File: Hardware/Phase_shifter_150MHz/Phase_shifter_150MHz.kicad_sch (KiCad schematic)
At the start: 19 parts, among them J1 SMA-J-P-H-ST-EM1, J2 SMA-J-P-H-ST-EM1, J3 SMA-J-P-H-ST-EM1, J4 0022272021, U1 SCPHS-180+, U2 LM358

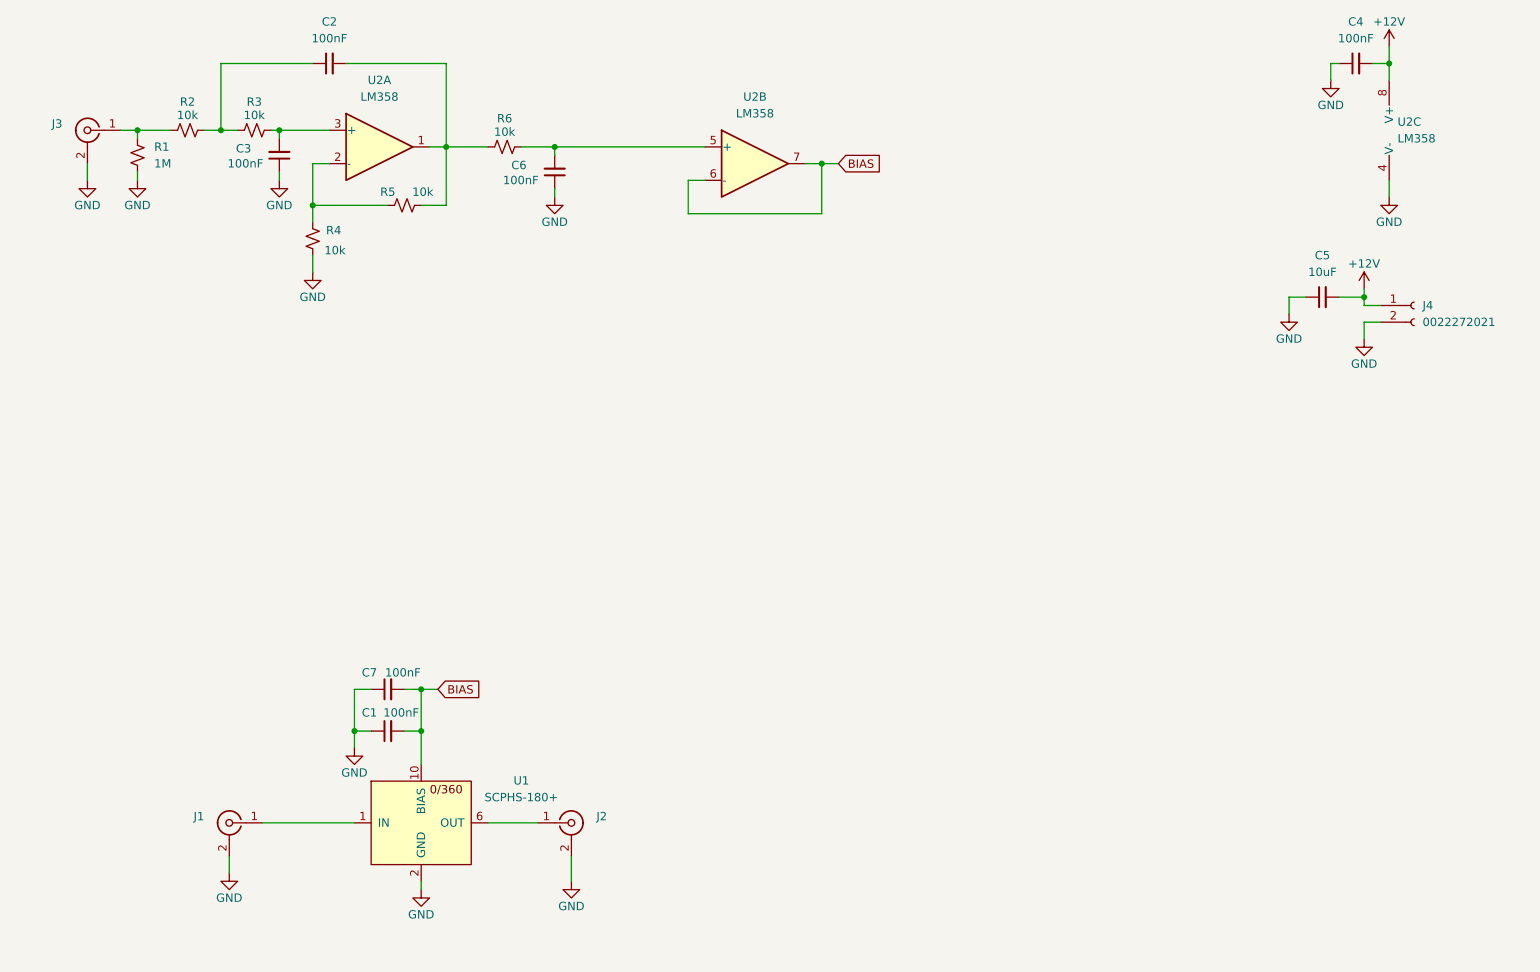
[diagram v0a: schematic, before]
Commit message: Working on Board layout for 150 MHz phase shifter
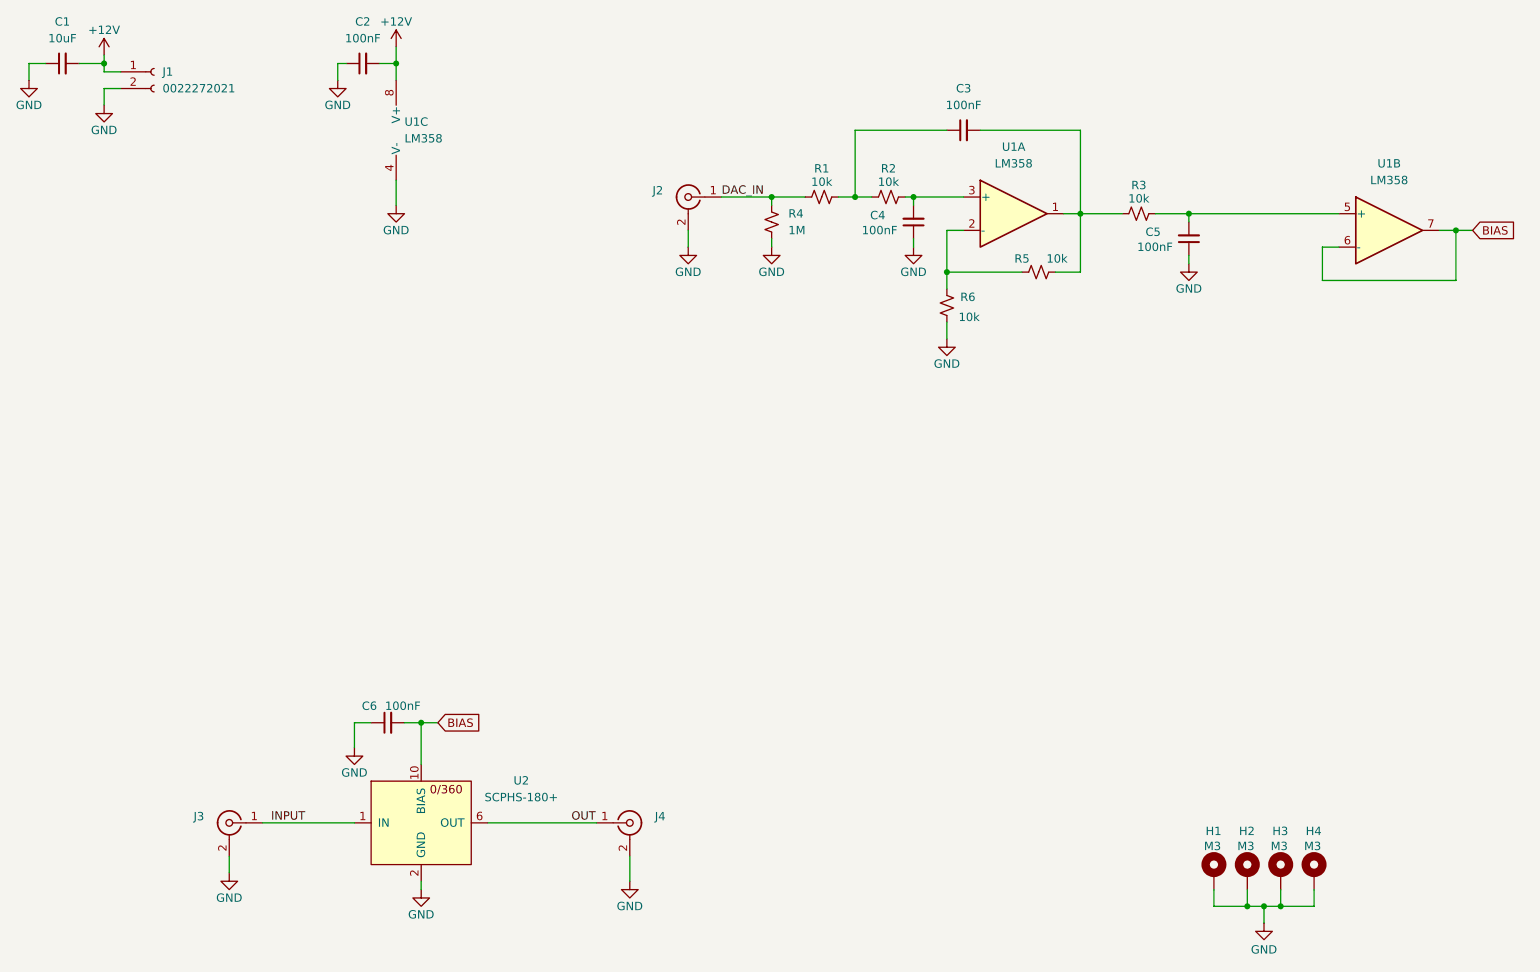
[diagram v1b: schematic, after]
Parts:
- removed C1: 100nF, Capacitor_SMD:C_0603_1608Metric, symbol Device:C_Small
- added H1, H2, H3, H4: M3, MountingHole:MountingHole_3.2mm_M3_DIN965_Pad, symbol Mechanical:MountingHole_Pad
- C1: renamed from C5; Digikey (none) -> 490-18663-1-ND; MPN (none) -> 490-18663-1-ND; Manufacturer (none) -> Murata Electronics
- C2: renamed from C4; footprint Capacitor_SMD:C_0603_1608Metric -> Capacitor_SMD:C_0805_2012Metric; Digikey 490-4779-1-ND -> 399-C0805C104K5RACTUCT-ND; MPN (none) -> C0805C104K5RACTU; Manufacturer (none) -> KEMET
- C3: renamed from C2; footprint Capacitor_SMD:C_0603_1608Metric -> Capacitor_SMD:C_0805_2012Metric; Digikey 490-4779-1-ND -> 399-C0805C104K5RACTUCT-ND; MPN (none) -> C0805C104K5RACTU; Manufacturer (none) -> KEMET
- C4: renamed from C3; footprint Capacitor_SMD:C_0603_1608Metric -> Capacitor_SMD:C_0805_2012Metric; Digikey 490-4779-1-ND -> 399-C0805C104K5RACTUCT-ND; MPN (none) -> C0805C104K5RACTU; Manufacturer (none) -> KEMET
- C5: renamed from C6; footprint Capacitor_SMD:C_0603_1608Metric -> Capacitor_SMD:C_0805_2012Metric; Digikey 490-4779-1-ND -> 399-C0805C104K5RACTUCT-ND; MPN (none) -> C0805C104K5RACTU; Manufacturer (none) -> KEMET
- C6: renamed from C7; footprint Capacitor_SMD:C_0603_1608Metric -> Capacitor_SMD:C_0805_2012Metric; Digikey 490-4779-1-ND -> 399-C0805C104K5RACTUCT-ND; MPN (none) -> C0805C104K5RACTU; Manufacturer (none) -> KEMET
- J1: renamed from J4; MPN (none) -> 0022272021; Manufacturer (none) -> Molex
- J2: renamed from J3; MPN (none) -> SMA-J-P-H-ST-EM1; Manufacturer (none) -> Samtec Inc.
- J3: renamed from J1; MPN (none) -> SMA-J-P-H-ST-EM1; Manufacturer (none) -> Samtec Inc.
- J4: renamed from J2; MPN (none) -> SMA-J-P-H-ST-EM1; Manufacturer (none) -> Samtec Inc.
- R1: renamed from R2; footprint Resistor_SMD:R_0603_1608Metric -> Resistor_SMD:R_0805_2012Metric; Digikey 311-10.0KHRCT-ND -> RMCF0805FT10K0CT-ND; MPN (none) -> RMCF0805FT10K0; Manufacturer (none) -> Stackpole Electronics Inc
- R2: renamed from R3; footprint Resistor_SMD:R_0603_1608Metric -> Resistor_SMD:R_0805_2012Metric; Digikey 311-10.0KHRCT-ND -> RMCF0805FT10K0CT-ND; MPN (none) -> RMCF0805FT10K0; Manufacturer (none) -> Stackpole Electronics Inc
- R3: renamed from R6; footprint Resistor_SMD:R_0603_1608Metric -> Resistor_SMD:R_0805_2012Metric; Digikey 311-10.0KHRCT-ND -> RMCF0805FT10K0CT-ND; MPN (none) -> RMCF0805FT10K0; Manufacturer (none) -> Stackpole Electronics Inc
- R4: renamed from R1; footprint Resistor_SMD:R_0603_1608Metric -> Resistor_SMD:R_0805_2012Metric; Digikey (none) -> 311-1.00MCRCT-ND; MPN (none) -> RC0805FR-071ML; Manufacturer (none) -> YAGEO
- R5: footprint Resistor_SMD:R_0603_1608Metric -> Resistor_SMD:R_0805_2012Metric; Digikey 311-10.0KHRCT-ND -> RMCF0805FT10K0CT-ND; MPN (none) -> RMCF0805FT10K0; Manufacturer (none) -> Stackpole Electronics Inc
- R6: renamed from R4; footprint Resistor_SMD:R_0603_1608Metric -> Resistor_SMD:R_0805_2012Metric; Digikey 311-10.0KHRCT-ND -> RMCF0805FT10K0CT-ND; MPN (none) -> RMCF0805FT10K0; Manufacturer (none) -> Stackpole Electronics Inc
- U1: renamed from U2; Digikey (none) -> 296-LM358DRCT-ND; MPN (none) -> LM358DR; Manufacturer (none) -> Texas Instruments
- U2: renamed from U1; Digikey (none) -> 3157-SCPHS-180+-ND; MPN (none) -> SCPHS-180+; Manufacturer (none) -> Mini-Circuits
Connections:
- net GND: now also H1.1, H2.1, H3.1, H4.1
- net DAC_IN: now reaches J2.1 (In), R1.1, R4.1
- net INPUT: now reaches J3.1 (In), U2.1 (IN)
- net OUT: now reaches J4.1 (In), U2.6 (OUT)
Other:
- moved on the sheet: C1, C2, C3, C4, C5, C6, J1, J2, J4, R1, R2, R3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
